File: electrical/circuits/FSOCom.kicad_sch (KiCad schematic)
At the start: 1 part, among them IC1 LCMXO3LF-1300E-5UWG36ITR

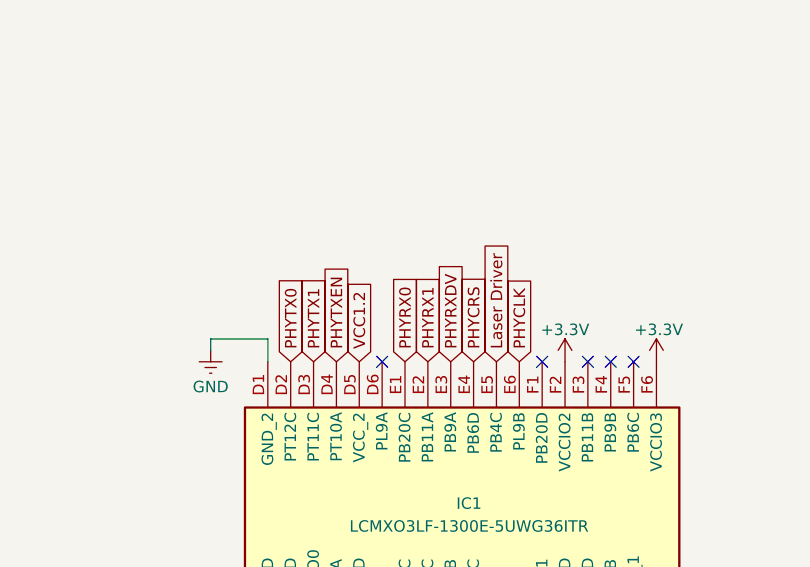
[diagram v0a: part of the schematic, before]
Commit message: Updated circuit schematics for 10BASE-T SNI mode
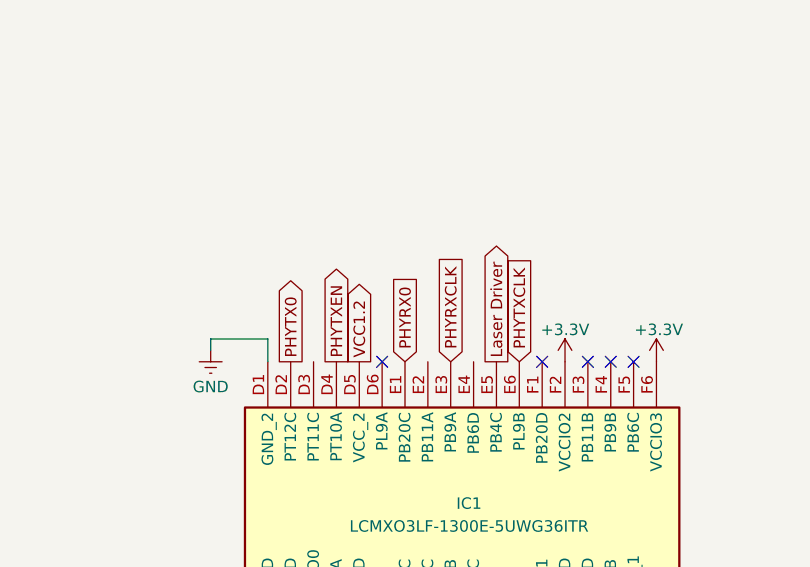
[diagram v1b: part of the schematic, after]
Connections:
- net PHYCLK renamed PHYTXCLK
- net PHYCRS: no longer names the net of IC1.E4 (PB6D)
- net PHYRX1: no longer names the net of IC1.E2 (PB11A)
- net PHYRXDV renamed PHYRXCLK
- net PHYTX1: no longer names the net of IC1.D3 (PT11C)
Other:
- company: Trystan Skye -> (none)
- title: Free Space Optical 100BASE-TX Ethernet Transceiver Circuit -> Free Space Optical 10BASE-T Ethernet Transceiver Circuit
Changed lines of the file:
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@@
 	(paper "A")
 	(title_block
-		(title "Free Space Optical 100BASE-TX Ethernet Transceiver Circuit")
-		(date "2025-07-15")
+		(title "Free Space Optical 10BASE-T Ethernet Transceiver Circuit")
+		(date "2025-07-22")
 		(rev "1")
-		(company "Trystan Skye")
 	)
 	(no_connect
@@
 		)
 	)
-	(global_label "PHYTX1"
-		(shape input)
-		(at 109.22 83.82 90)
-		(fields_autoplaced yes)
-		(effects
-			(font
-				(size 1.27 1.27)
-			)
-			(justify left)
-		)
-		(property "Intersheetrefs" "${INTERSHEET_REFS}"
-			(at 109.22 73.7591 90)
-			(effects
-				(font
-					(size 1.27 1.27)
-				)
-				(justify left)
-				(hide yes)
-			)
-		)
-	)
 	(global_label "ADC2"
 		(shape input)
@@
 	)
 	(global_label "PHYTXEN"
-		(shape input)
+		(shape output)
 		(at 111.76 83.82 90)
 		(fields_autoplaced yes)
@@
 		)
 	)
-	(global_label "PHYRX1"
-		(shape input)
-		(at 121.92 83.82 90)
-		(fields_autoplaced yes)
-		(effects
-			(font
-				(size 1.27 1.27)
-			)
-			(justify left)
-		)
-		(property "Intersheetrefs" "${INTERSHEET_REFS}"
-			(at 121.92 73.4567 90)
+	(global_label "PHYRXCLK"
+		(shape input)
+		(at 124.46 83.82 90)
+		(fields_autoplaced yes)
+		(effects
+			(font
+				(size 1.27 1.27)
+			)
+			(justify left)
+		)
+		(property "Intersheetrefs" "${INTERSHEET_REFS}"
+			(at 124.46 71.0981 90)
 			(effects
 				(font
@@
 	)
 	(global_label "VCC1.2"
-		(shape input)
+		(shape output)
 		(at 114.3 83.82 90)
 		(fields_autoplaced yes)
@@
 		)
 	)
-	(global_label "PHYRXDV"
-		(shape input)
-		(at 124.46 83.82 90)
-		(fields_autoplaced yes)
-		(effects
-			(font
-				(size 1.27 1.27)
-			)
-			(justify left)
-		)
-		(property "Intersheetrefs" "${INTERSHEET_REFS}"
-			(at 124.46 72.3076 90)
-			(effects
-				(font
-					(size 1.27 1.27)
-				)
-				(justify left)
-				(hide yes)
-			)
-		)
-	)
 	(global_label "PHYRX0"
 		(shape input)
@@
 		)
 	)
-	(global_label "PHYCLK"
+	(global_label "PHYTXCLK"
 		(shape input)
 		(at 132.08 83.82 90)
@@
 		)
 		(property "Intersheetrefs" "${INTERSHEET_REFS}"
-			(at 132.08 73.5776 90)
-			(effects
-				(font
-					(size 1.27 1.27)
-				)
-				(justify left)
-				(hide yes)
-			)
-		)
-	)
-	(global_label "PHYCRS"
-		(shape input)
-		(at 127 83.82 90)
-		(fields_autoplaced yes)
-		(effects
-			(font
-				(size 1.27 1.27)
-			)
-			(justify left)
-		)
-		(property "Intersheetrefs" "${INTERSHEET_REFS}"
-			(at 127 73.3962 90)
+			(at 132.08 71.4005 90)
 			(effects
 				(font
@@
 	)
 	(global_label "Laser Driver"
-		(shape input)
+		(shape output)
 		(at 129.54 83.82 90)
 		(fields_autoplaced yes)
@@
 	)
 	(global_label "PHYTX0"
-		(shape input)
+		(shape output)
 		(at 106.68 83.82 90)
 		(fields_autoplaced yes)
